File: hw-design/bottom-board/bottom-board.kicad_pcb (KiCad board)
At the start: 2 copper layers, 172 x 140.5 mm, 240 parts, among them J1 RJ45_LEDS, J2 JACK_TRS_6PINS, J3 JACK_TRS_6PINS, J4 JACK_TRS_6PINS, J5 JACK_TRS_6PINS, J6 JACK_TRS_6PINS, K1 IM03, K2 IM03, P1 USB_B, P2 USB_A, P3 DIN_5, P4 DIN_5, P5 BARREL_JACK, P6 CONN_02X10, P7 CONN_01X10, P9 CONN_01X03, Q1 J112, Q10 2N7002, Q11 2N7002, Q12 2N7002, Q13 2N7002, Q14 2N7002, Q15 2N7002, Q2 J112, Q3 2N7002, Q4 2N7002, Q5 J112, Q6 J112, Q7 2N7002, Q8 2N7002, Q9 2N7002, SW1 SW_PUSH, U1 MCP1754ST-5002E/MB, U10 LM4811, U11 RT9701, U12 6N137S, U13 ISL83491, U2 KA7809, U3 NCP1117ST50T3G, U4 NCP1117ST33T3G, U5 CS4245, U6 ICnova_A20_SODIMM, U7 LM4562, U8 LM4562, U9 LM4562

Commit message: pcb: tracing HMI tracks (wip)
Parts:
- moved P6 5.23 mm to (83.3, 67.2)
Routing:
- net UART_TX3_HMI: track 0.00 -> 88.0 mm, vias 0 -> 2
- net UART_RX3_HMI: track 0.00 -> 84.5 mm, vias 0 -> 2
- net UART_RTS3_HMI: track 0.00 -> 80.1 mm, vias 0 -> 2
- net UART_CTS3_HMI: track 0.00 -> 75.1 mm, vias 0 -> 2
- net SPI0_MISO_HMI: track 0.00 -> 49.6 mm
- net SPI0_MOSI_HMI: track 0.00 -> 47.5 mm
- net SPI0_CLK_HMI: track 0.00 -> 45.5 mm
- net SPI0_CS0_HMI: track 0.00 -> 43.3 mm

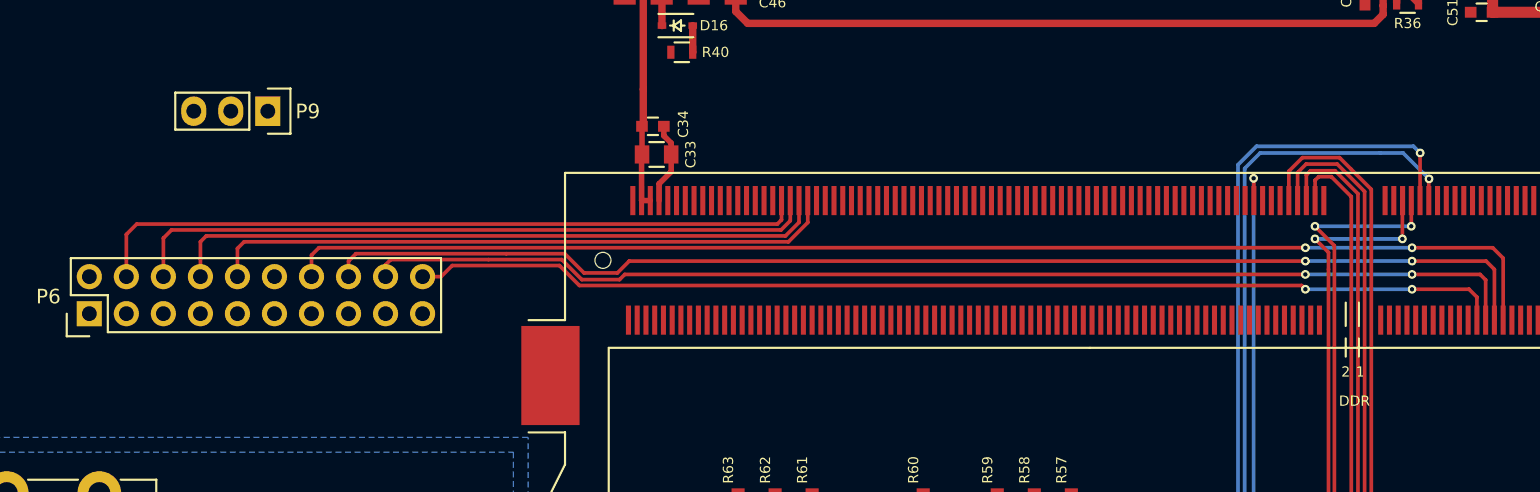
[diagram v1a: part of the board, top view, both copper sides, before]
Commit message: pcb: tracing HMI tracks done
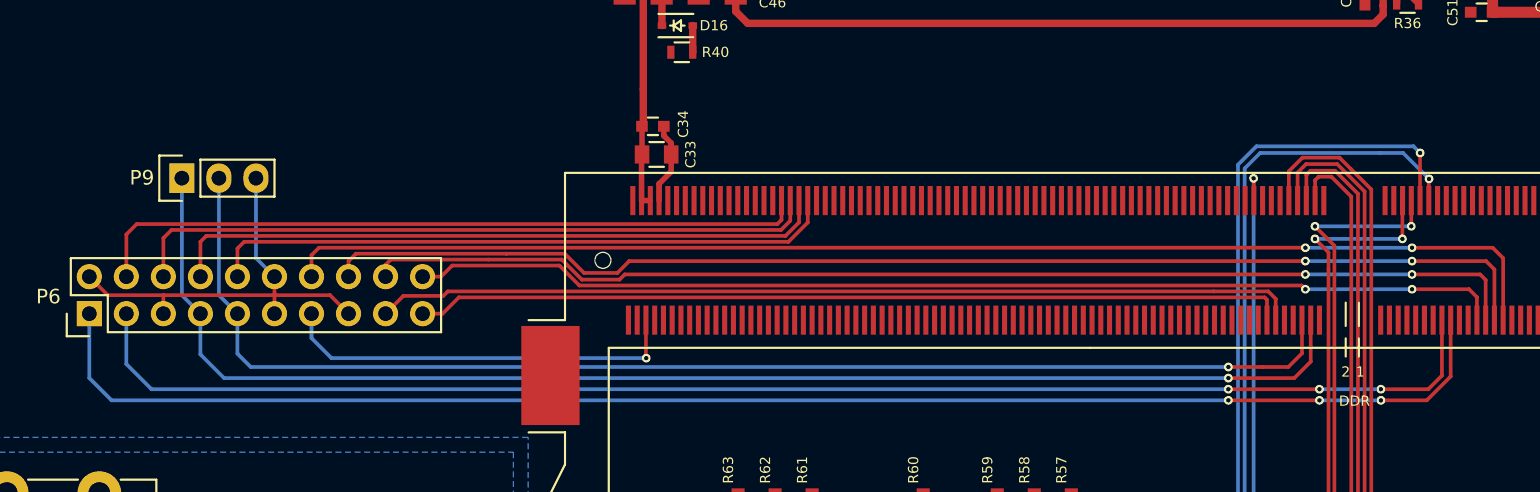
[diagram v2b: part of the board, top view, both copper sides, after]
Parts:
- moved P9 7.47 mm to (89.7, 57.9), turned to 90 degrees
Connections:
- P6 pad 1: POWER_BUTTON -> RFU_02_HMI
- P6 pad 11: UART_TX0_CLI -> GNDD
- P6 pad 13: GNDD -> POWER_BUTTON
- P6 pad 15: RFU_01_HMI -> GNDD
- P6 pad 17: RFU_02_HMI -> I2C_SCL_HMI
- P6 pad 19: GNDD -> I2C_SDA_HMI
- P6 pad 3: GNDD -> RFU_01_HMI
- P6 pad 5: I2C_SDA_HMI -> GNDD
- P6 pad 7: I2C_SCL_HMI -> UART_TX0_CLI
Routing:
- net RFU_02_HMI: track 0.00 -> 103.0 mm, vias 0 -> 3
- net RFU_01_HMI: track 0.00 -> 98.6 mm, vias 0 -> 3
- net UART_TX0_CLI: track 0.00 -> 92.8 mm, vias 0 -> 1
- net UART_RX0_CLI: track 0.00 -> 88.6 mm, vias 0 -> 1
- net I2C_SCL_HMI: track 0.00 -> 63.4 mm
- net I2C_SDA_HMI: track 0.00 -> 59.8 mm
- net GNDD: track 175.0 -> 205.2 mm
- net POWER_BUTTON: track 0.00 -> 27.8 mm, vias 0 -> 1

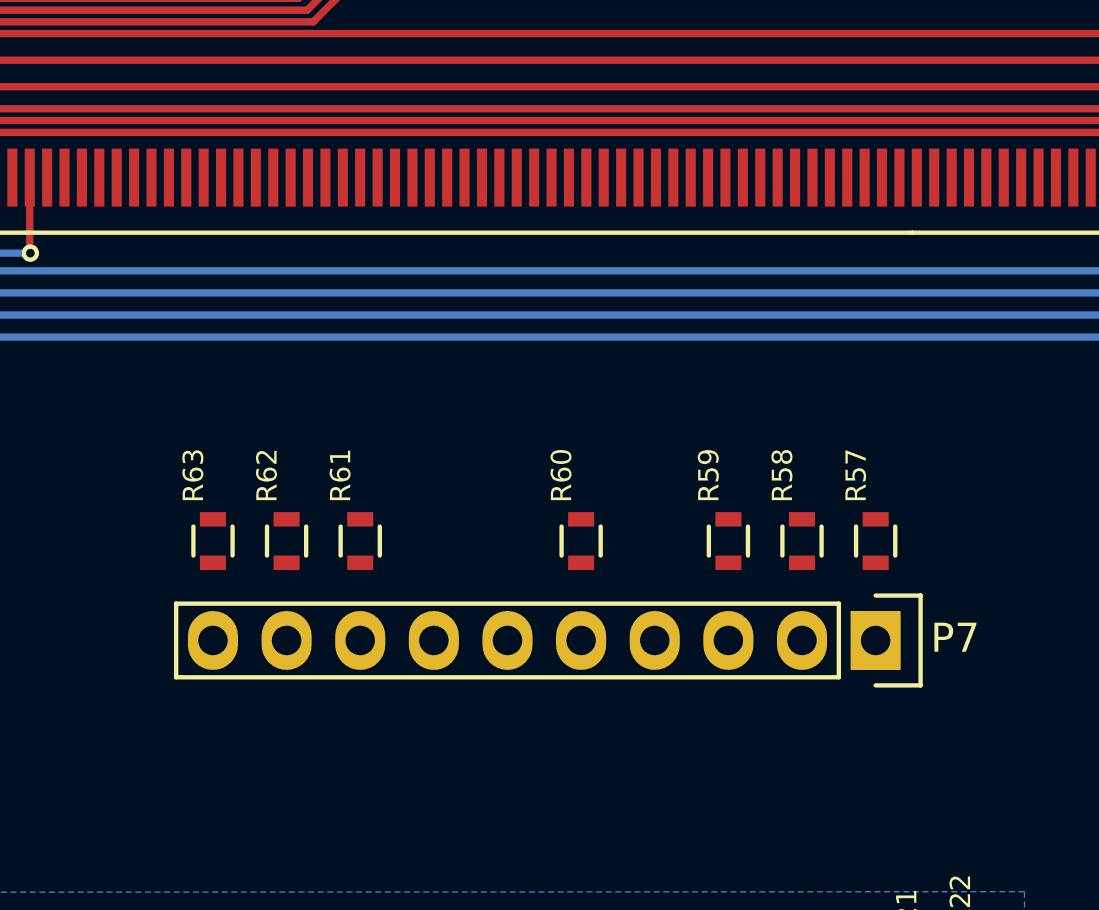
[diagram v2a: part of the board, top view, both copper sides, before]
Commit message: pcb: sdcard tracks done
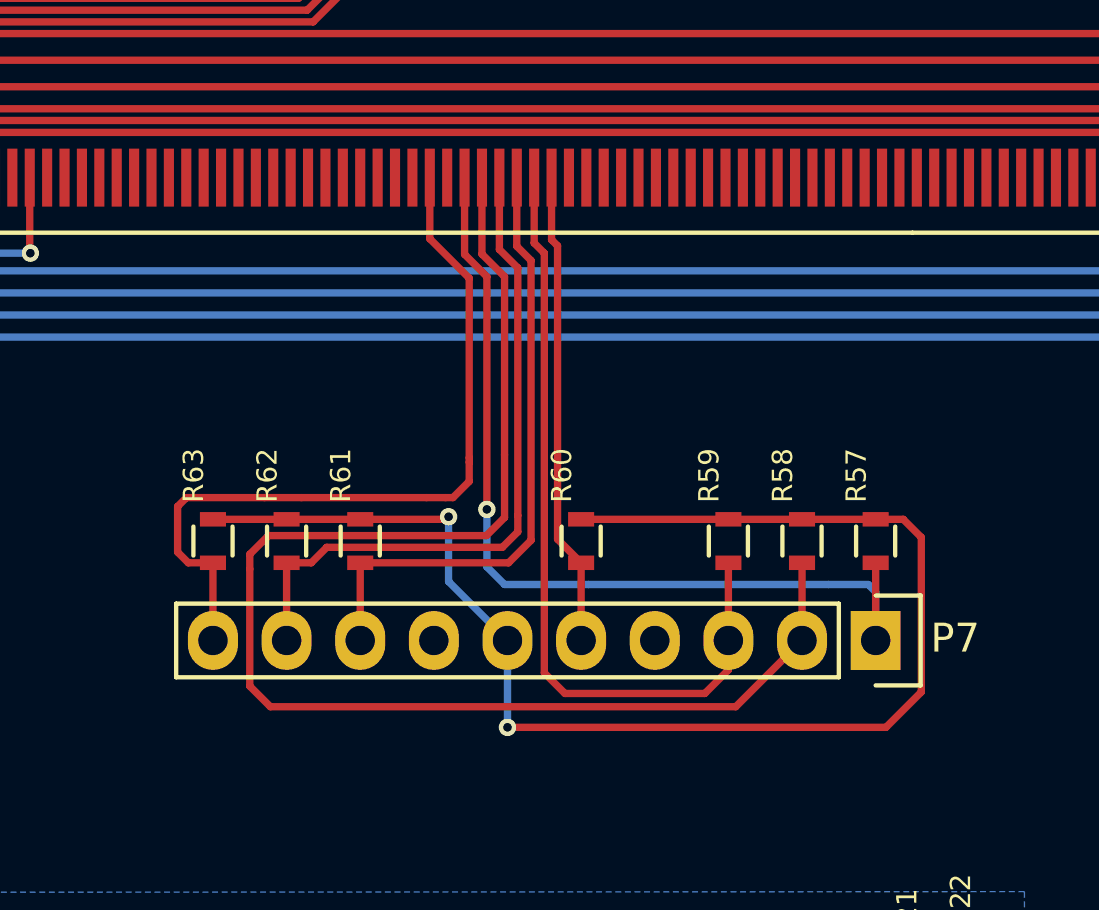
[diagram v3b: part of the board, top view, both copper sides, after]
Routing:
- net SD0_D3: track 0.00 -> 48.9 mm
- net +3V3: track 67.1 -> 115.5 mm, vias 2 -> 4
- net SD0_D2: track 0.00 -> 31.9 mm, vias 0 -> 1
- net SD0_CMD: track 0.00 -> 27.9 mm
- net SD0_DETECT: track 0.00 -> 27.3 mm
- net SD0_D1: track 0.00 -> 23.6 mm
- net SD0_D0: track 0.00 -> 21.6 mm
- net SD0_CLK: track 0.00 -> 16.4 mm

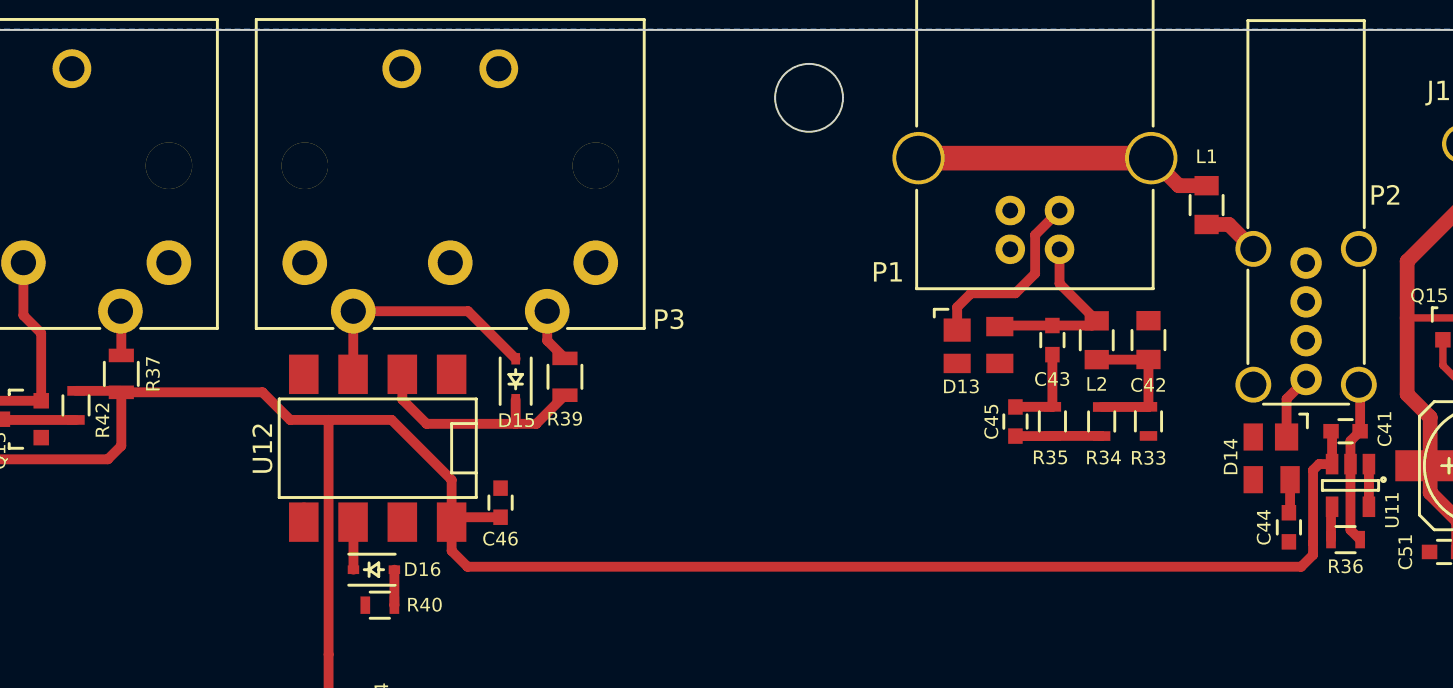
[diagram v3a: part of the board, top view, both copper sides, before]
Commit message: pcb: moving +5V track up board side
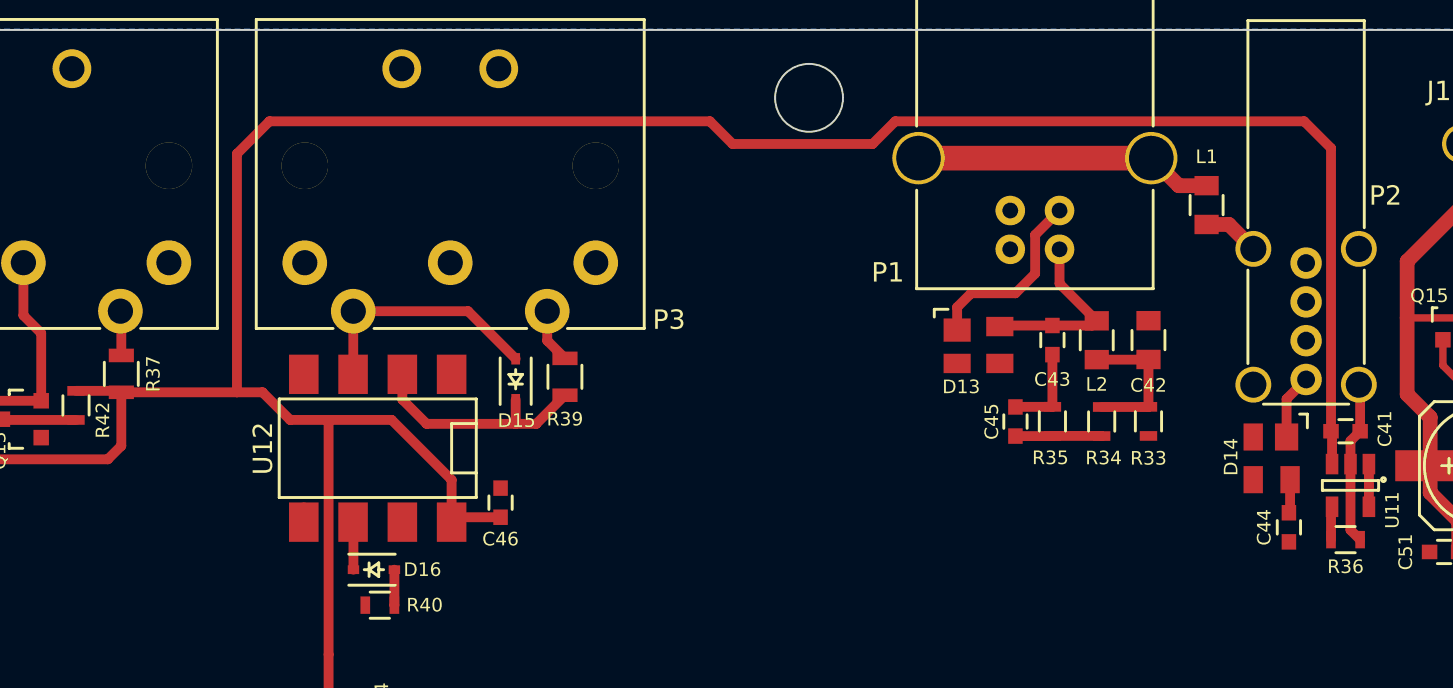
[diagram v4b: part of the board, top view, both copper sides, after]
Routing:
- net +5V: track 160.5 -> 194.1 mm
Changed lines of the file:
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@@
     (thickness 1.6)
     (drawings 17)
-    (tracks 1496)
+    (tracks 1498)
     (zones 0)
     (modules 240)
@@
   )
   (setup
-    (last_trace_width 0.254)
+    (last_trace_width 0.508)
     (user_trace_width 0.2032)
     (user_trace_width 0.254)
@@
   (segment (start 123.2248 55.4576) (end 123.2248 56.2356) (width 0.381) (layer F.Cu) (net 6))
   (segment (start 122.7208 54.3052) (end 122.7208 54.9536) (width 0.381) (layer F.Cu) (net 6))
+  (segment (start 172.986 40.259) (end 172.986 25.666) (width 0.508) (layer F.Cu) (net 7) (status 400000))
+  (segment (start 116.586 25.9588) (end 116.586 38.252) (width 0.508) (layer F.Cu) (net 7))
+  (segment (start 118.2624 24.2824) (end 116.586 25.9588) (width 0.508) (layer F.Cu) (net 7))
+  (segment (start 140.97 24.2824) (end 118.2624 24.2824) (width 0.508) (layer F.Cu) (net 7))
+  (segment (start 142.1384 25.4508) (end 140.97 24.2824) (width 0.508) (layer F.Cu) (net 7))
+  (segment (start 149.352 25.4508) (end 142.1384 25.4508) (width 0.508) (layer F.Cu) (net 7))
+  (segment (start 150.5204 24.2824) (end 149.352 25.4508) (width 0.508) (layer F.Cu) (net 7))
+  (segment (start 171.6024 24.2824) (end 150.5204 24.2824) (width 0.508) (layer F.Cu) (net 7))
+  (segment (start 172.986 25.666) (end 171.6024 24.2824) (width 0.508) (layer F.Cu) (net 7))
   (segment (start 105.2576 95.516) (end 104.636 95.516) (width 0.3048) (layer F.Cu) (net 7))
   (segment (start 102.108 98.298) (end 100.1656 98.298) (width 0.3048) (layer F.Cu) (net 7))
@@
   (segment (start 201.422 80.55356) (end 201.40168 80.53324) (width 1.27) (layer F.Cu) (net 7))
   (segment (start 201.422 87.1728) (end 201.422 80.55356) (width 1.27) (layer F.Cu) (net 7))
-  (segment (start 172.3722 41.953) (end 172.0596 42.2656) (width 0.508) (layer F.Cu) (net 7))
-  (segment (start 172.0596 42.2656) (end 172.0596 46.0248) (width 0.508) (layer F.Cu) (net 7))
-  (segment (start 173.04 41.953) (end 172.3722 41.953) (width 0.508) (layer F.Cu) (net 7))
   (segment (start 121.1928 56.2676) (end 121.2248 56.2356) (width 0.381) (layer F.Cu) (net 7))
   (segment (start 121.1928 59.4) (end 121.1928 56.2676) (width 0.381) (layer F.Cu) (net 7))
@@
   (segment (start 127.65278 42.76598) (end 127.65278 44.9453) (width 0.508) (layer F.Cu) (net 7))
   (segment (start 119.3292 39.6748) (end 121.3104 39.6748) (width 0.508) (layer F.Cu) (net 7))
+  (segment (start 116.586 38.252) (end 117.9064 38.252) (width 0.508) (layer F.Cu) (net 7))
   (segment (start 117.9064 38.252) (end 119.3292 39.6748) (width 0.508) (layer F.Cu) (net 7))
-  (segment (start 110.6252 38.252) (end 117.9064 38.252) (width 0.508) (layer F.Cu) (net 7))
+  (segment (start 110.6252 38.252) (end 116.586 38.252) (width 0.508) (layer F.Cu) (net 7))
   (segment (start 121.3104 39.6748) (end 121.3104 51.7652) (width 0.508) (layer F.Cu) (net 7))
   (segment (start 121.3104 54.2156) (end 121.2208 54.3052) (width 0.508) (layer F.Cu) (net 7))
   (segment (start 121.3104 51.7652) (end 121.3104 54.2156) (width 0.508) (layer F.Cu) (net 7))
-  (segment (start 172.0596 46.6344) (end 171.45 47.244) (width 0.508) (layer F.Cu) (net 7))
-  (segment (start 171.45 47.244) (end 128.4732 47.244) (width 0.508) (layer F.Cu) (net 7))
-  (segment (start 128.4732 47.244) (end 127.65278 46.42358) (width 0.508) (layer F.Cu) (net 7))
-  (segment (start 127.65278 46.42358) (end 127.65278 44.9453) (width 0.508) (layer F.Cu) (net 7))
-  (segment (start 172.0596 46.0248) (end 172.0596 46.6344) (width 0.508) (layer F.Cu) (net 7))
   (segment (start 98.8396 41.1308) (end 99.4156 41.7068) (width 0.508) (layer F.Cu) (net 7))
   (segment (start 99.4156 41.7068) (end 109.9312 41.7068) (width 0.508) (layer F.Cu) (net 7))

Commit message: pcb: updating netlist
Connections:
- P6 pad 14: UART_TX3_HMI -> UART_RX3_HMI
- P6 pad 16: UART_RX3_HMI -> UART_TX3_HMI
- P6 pad 18: UART_RTS3_HMI -> UART_CTS3_HMI
- P6 pad 20: UART_CTS3_HMI -> UART_RTS3_HMI
- U6 pad 12: UART_TX3_HMI -> UART_TX_CHAIN
- U6 pad 14: UART_RX3_HMI -> UART_RX_CHAIN
- U6 pad 149: UART_DE_CHAIN -> UART_RTS3_HMI
- U6 pad 151: UART_RE_CHAIN -> UART_CTS3_HMI
- U6 pad 153: UART_TX_CHAIN -> UART_TX3_HMI
- U6 pad 155: UART_RX_CHAIN -> UART_RX3_HMI
- U6 pad 16: UART_RTS3_HMI -> UART_DE_CHAIN
- U6 pad 18: UART_CTS3_HMI -> UART_RE_CHAIN
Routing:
- net UART_TX3_HMI: track 88.0 -> 0.00 mm, vias 2 -> 0
- net UART_RX3_HMI: track 84.5 -> 0.00 mm, vias 2 -> 0
- net UART_RTS3_HMI: track 80.1 -> 0.00 mm, vias 2 -> 0
- net UART_CTS3_HMI: track 75.1 -> 8.02 mm, vias 2 -> 0
